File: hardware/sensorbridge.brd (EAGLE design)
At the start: 55.9 x 53.3 mm, 14 parts

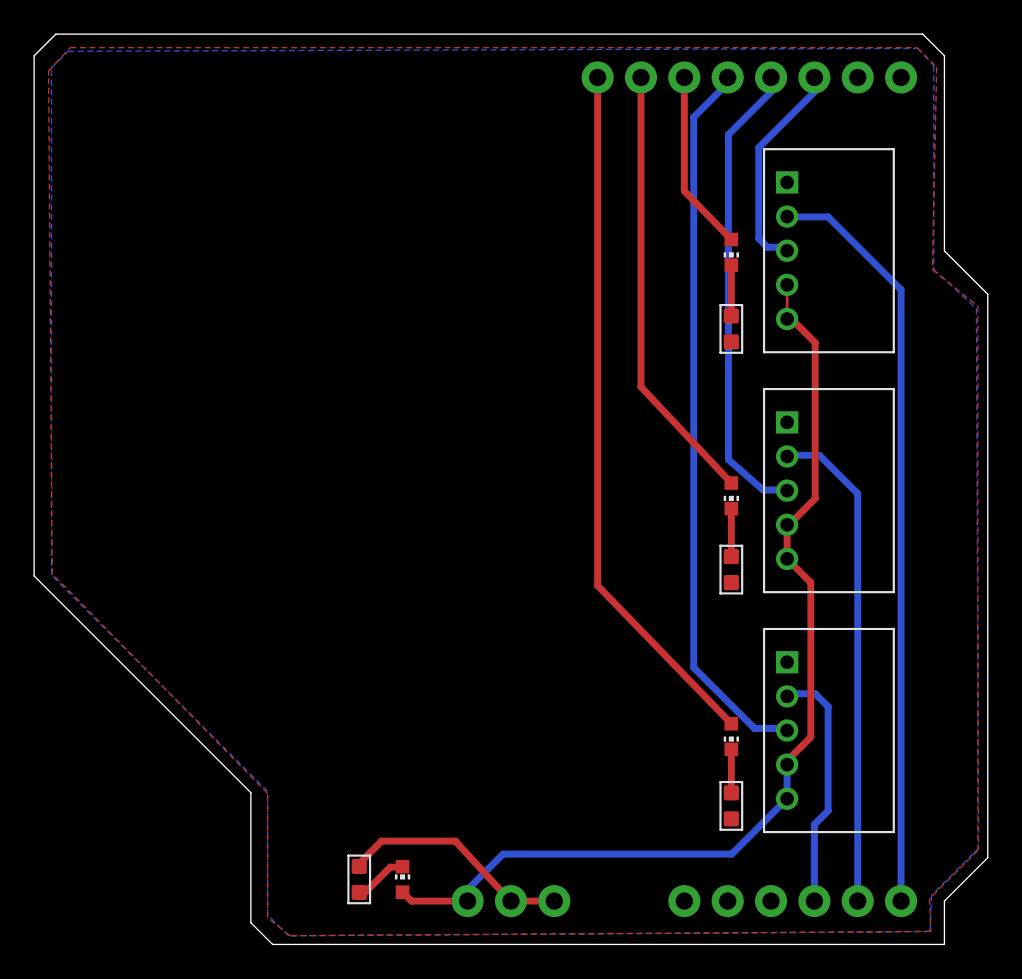
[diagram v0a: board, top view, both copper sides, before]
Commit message: Made sensor connection through GND instead of VCC, added pulldown resistors to DATA lines
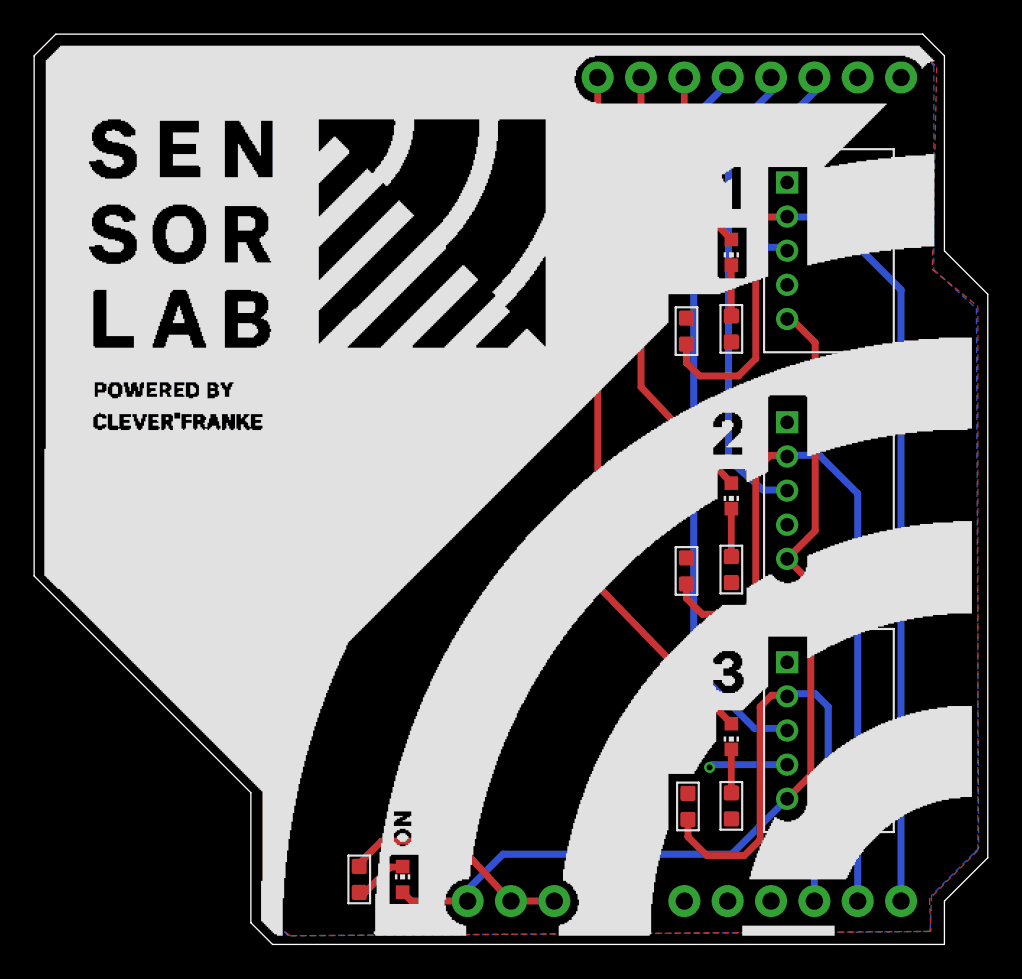
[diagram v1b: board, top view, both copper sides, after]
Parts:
- added R4, R5, R6: 10K, Seeed-OPL-Resistor:R0603
- R1, R2, R3, R8: value (none) -> 470
- renumbered ANALOG to ARDUINO_ANALOG, JP2 to ARDUINO_DIGITAL, PWR to ARDUINO_SUPPLY
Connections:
- net +5V: no longer INPUT_1.4, INPUT_2.4, INPUT_3.4
- net GND: now also INPUT_1.4, INPUT_2.4, INPUT_3.4, R4.1, R5.1, R6.1
- net S1_DATA: now also R4.2
- net S2_DATA: now also R5.2
- net S3_DATA: now also R6.2
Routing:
- net S3_DATA: track 14.5 -> 30.3 mm
- net S1_DATA: track 44.3 -> 60.0 mm
- net S2_DATA: track 29.0 -> 44.4 mm
- net GND: track 13.7 -> 18.3 mm, vias 0 -> 1
- net +5V: track 58.5 -> 56.4 mm
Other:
- board text added: "SENSORBRIDGE V1.2 SENSORLAB.NL"
- board text removed: "C:/Users/Wilco/Desktop/sensorbridge-art/sensorbridge-bottom.bmp"
- board text removed: "SENSORBRIDGE V1.1 SENSORLAB.NL"

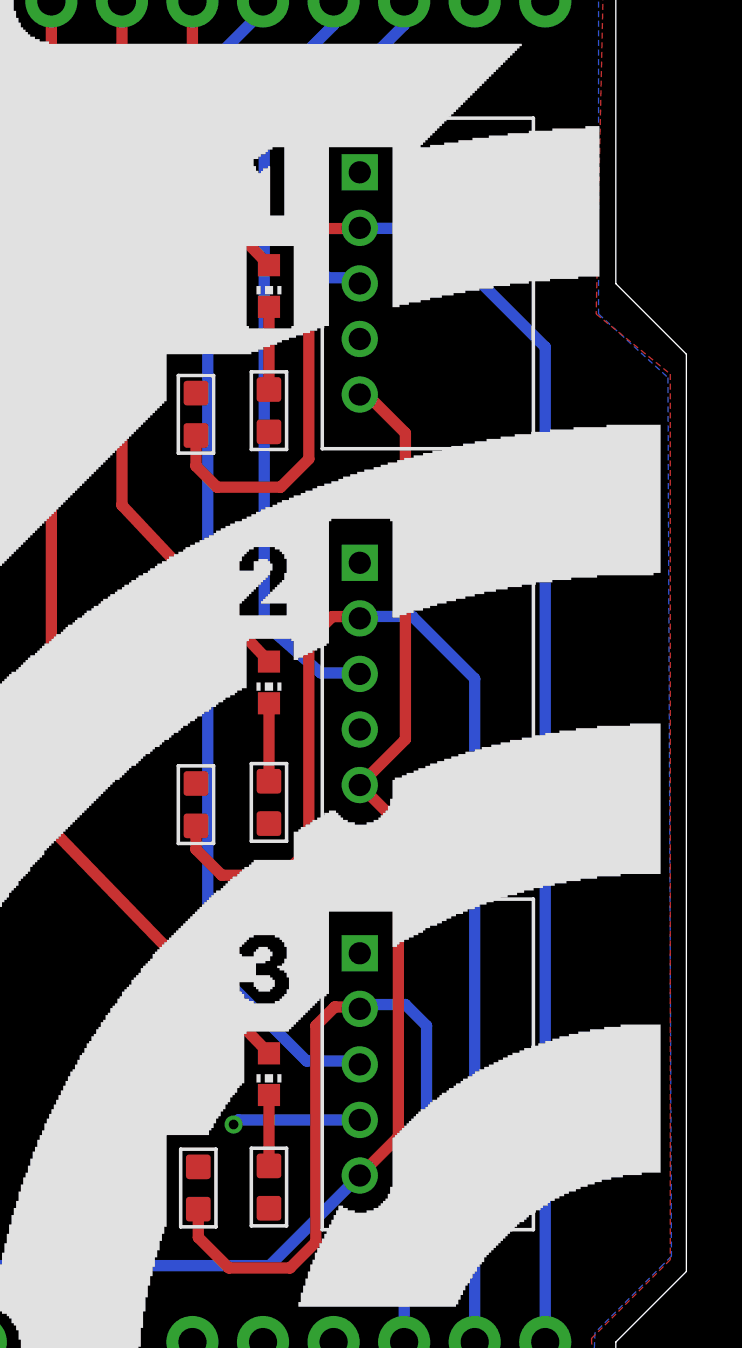
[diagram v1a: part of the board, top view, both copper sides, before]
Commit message: Fixed DRC error
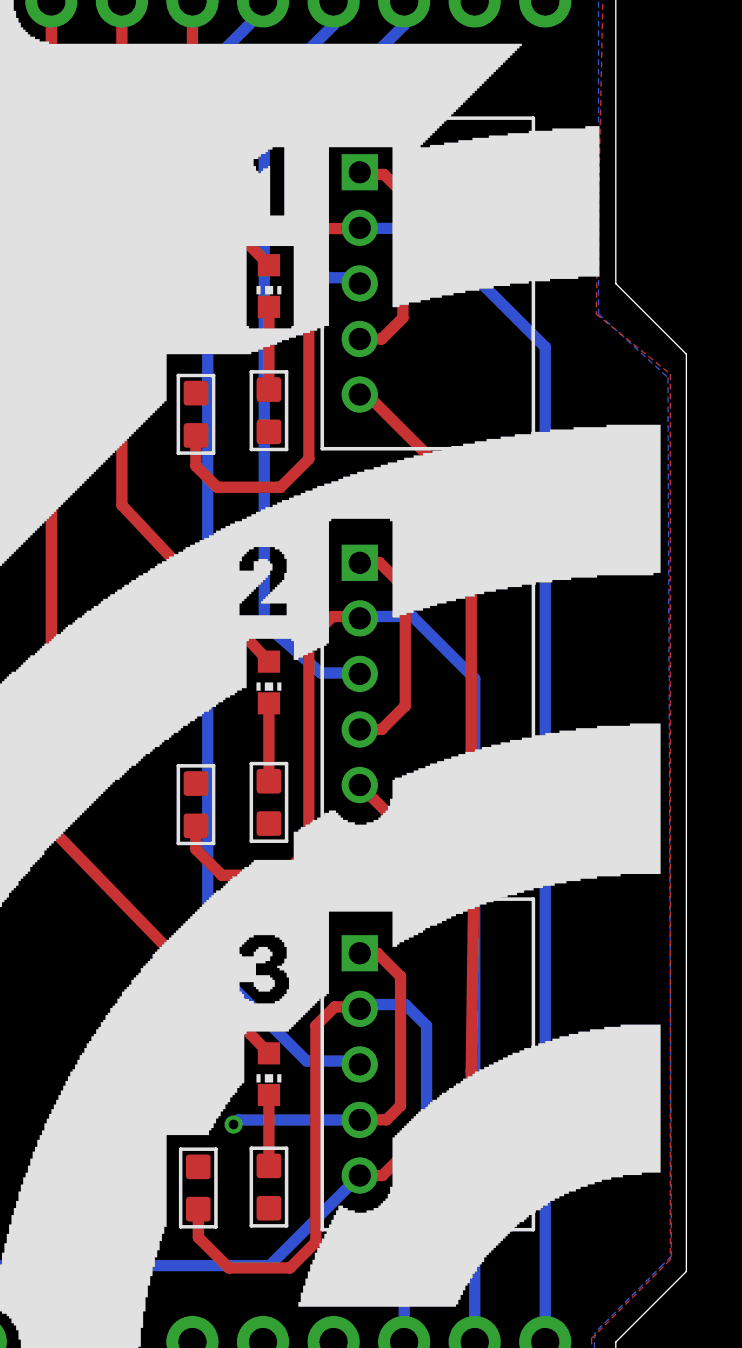
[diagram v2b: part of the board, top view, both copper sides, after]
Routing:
- net GND: track 18.3 -> 42.9 mm
- net +5V: track 56.4 -> 63.5 mm
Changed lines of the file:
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@@
 <layer number="199" name="Contour" color="7" fill="1" visible="no" active="yes"/>
 <layer number="200" name="TOPsilk" color="58" fill="1" visible="no" active="yes"/>
-<layer number="201" name="BOTTOMsilk" color="50" fill="1" visible="yes" active="yes"/>
+<layer number="201" name="BOTTOMsilk" color="50" fill="1" visible="no" active="yes"/>
 <layer number="202" name="202bmp" color="2" fill="10" visible="no" active="yes"/>
 <layer number="203" name="203bmp" color="1" fill="10" visible="no" active="yes"/>
@@
 <wire x1="39.699609375" y1="10.577190625" x2="39.535378125" y2="10.412959375" width="0.4064" layer="16"/>
 <via x="39.535378125" y="10.412959375" extent="1-16" drill="0.35"/>
-<wire x1="44.07781875" y1="10.577190625" x2="44.07781875" y2="16.577190625" width="0" layer="19" extent="1-1"/>
-<wire x1="44.07781875" y1="30.634059375" x2="44.07781875" y2="24.634059375" width="0" layer="19" extent="1-1"/>
+<wire x1="44.07781875" y1="16.577190625" x2="44.715346875" y2="16.577190625" width="0.4064" layer="1"/>
+<wire x1="44.715346875" y1="16.577190625" x2="45.5461125" y2="15.746425" width="0.4064" layer="1"/>
+<wire x1="45.5461125" y1="15.746425" x2="45.5461125" y2="11.090225" width="0.4064" layer="1"/>
+<wire x1="45.5461125" y1="11.090225" x2="45.0381625" y2="10.582275" width="0.4064" layer="1"/>
+<wire x1="45.0381625" y1="10.582275" x2="44.082903125" y2="10.582275" width="0.4064" layer="1"/>
+<wire x1="44.082903125" y1="10.582275" x2="44.07781875" y2="10.577190625" width="0.4064" layer="1"/>
+<wire x1="44.07781875" y1="24.634059375" x2="44.86736875" y2="24.634059375" width="0.4064" layer="1"/>
+<wire x1="44.86736875" y1="24.634059375" x2="45.715428125" y2="25.48211875" width="0.4064" layer="1"/>
+<wire x1="45.715428125" y1="25.48211875" x2="45.715428125" y2="29.715028125" width="0.4064" layer="1"/>
+<wire x1="45.715428125" y1="29.715028125" x2="44.7841875" y2="30.64626875" width="0.4064" layer="1"/>
+<wire x1="44.7841875" y1="30.64626875" x2="44.090028125" y2="30.64626875" width="0.4064" layer="1"/>
+<wire x1="44.090028125" y1="30.64626875" x2="44.07781875" y2="30.634059375" width="0.4064" layer="1"/>
+<wire x1="44.07781875" y1="38.690928125" x2="44.870975" y2="38.690928125" width="0.4064" layer="1"/>
+<wire x1="44.870975" y1="38.690928125" x2="45.63076875" y2="39.450721875" width="0.4064" layer="1"/>
+<wire x1="45.63076875" y1="39.450721875" x2="45.63076875" y2="43.93760625" width="0.4064" layer="1"/>
+<wire x1="45.63076875" y1="43.93760625" x2="44.953503125" y2="44.614871875" width="0.4064" layer="1"/>
+<wire x1="44.953503125" y1="44.614871875" x2="44.153875" y2="44.614871875" width="0.4064" layer="1"/>
+<wire x1="44.153875" y1="44.614871875" x2="44.07781875" y2="44.690928125" width="0.4064" layer="1"/>
 </signal>
 <signal name="N$1">
@@
 <wire x1="27.432" y1="5.334" x2="40.834628125" y2="5.334" width="0.4064" layer="16"/>
 <wire x1="40.834628125" y1="5.334" x2="44.07781875" y2="8.577190625" width="0.4064" layer="16"/>
-<wire x1="44.07781875" y1="22.634059375" x2="45.466" y2="21.245878125" width="0.4064" layer="1"/>
+<wire x1="48.175065625" y1="18.53681875" x2="44.07781875" y2="22.634059375" width="0.4064" layer="1"/>
 <wire x1="44.335071875" y1="36.690928125" x2="44.07781875" y2="36.690928125" width="0.4064" layer="1"/>
-<wire x1="44.335071875" y1="36.690928125" x2="45.72" y2="35.306" width="0.4064" layer="1"/>
-<wire x1="45.466" y1="9.965371875" x2="44.07781875" y2="8.577190625" width="0.4064" layer="1"/>
-<wire x1="45.466" y1="21.245878125" x2="45.466" y2="9.965371875" width="0.4064" layer="1"/>
-<wire x1="45.72" y1="24.276240625" x2="44.07781875" y2="22.634059375" width="0.4064" layer="1"/>
-<wire x1="45.72" y1="35.306" x2="45.72" y2="24.276240625" width="0.4064" layer="1"/>
+<wire x1="44.335071875" y1="36.690928125" x2="48.09043125" y2="32.935575" width="0.4064" layer="1"/>
+<wire x1="48.09040625" y1="12.335803125" x2="48.08585625" y2="11.767490625" width="0.4064" layer="1"/>
+<wire x1="48.08585625" y1="11.767490625" x2="45.461453125" y2="9.1430875" width="0.4064" layer="1"/>
+<wire x1="45.461453125" y1="9.1430875" x2="45.461453125" y2="9.143084375" width="0.4064" layer="1"/>
+<wire x1="45.461453125" y1="9.143084375" x2="44.895559375" y2="8.577190625" width="0.4064" layer="1"/>
+<wire x1="44.895559375" y1="8.577190625" x2="44.07781875" y2="8.577190625" width="0.4064" layer="1"/>
+<wire x1="48.175065625" y1="18.53681875" x2="48.09040625" y2="12.335803125" width="0.4064" layer="1"/>
+<wire x1="48.09043125" y1="21.415175" x2="48.175065625" y2="18.53681875" width="0.4064" layer="1"/>
+<wire x1="48.09043125" y1="32.935575" x2="48.09043125" y2="21.415175" width="0.4064" layer="1"/>
 </signal>
 <signal name="S1_CONN">
